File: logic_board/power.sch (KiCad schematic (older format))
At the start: 17 parts, among them J4 Amphenol 124015, J5 Batt, SW5 Power, U4 SPX3819M5-L-3-3, U5 BQ24090DGQR

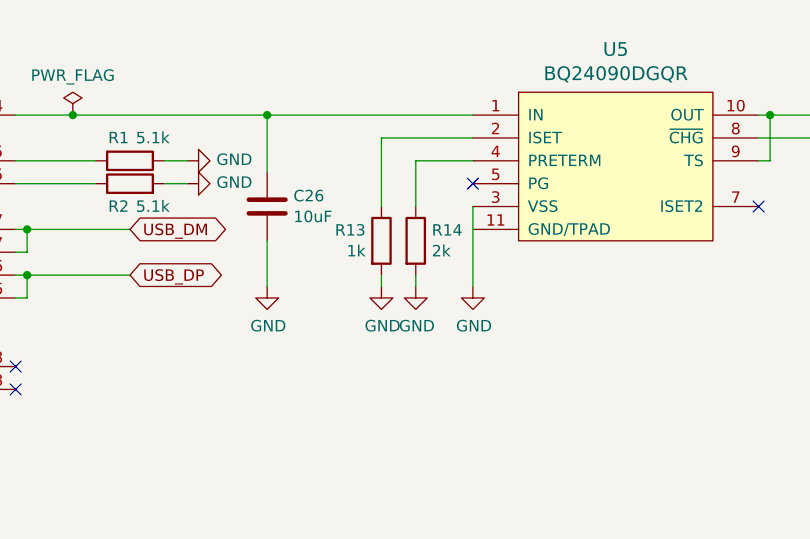
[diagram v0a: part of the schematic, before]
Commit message: Connect the thermal pad of the charger per datasheet recommendations
- Added a separate pin 11 for the thermal pad in the custom symbol.
- Ground the thermal pad.
- Add a bunch of vias to conduct heat through the board.
- Add a copper pour on the back side of the board to radiate heat.

Although the backside pour is at ground potential, I have added keepouts
around all ground via in its area to avoid ground loops.
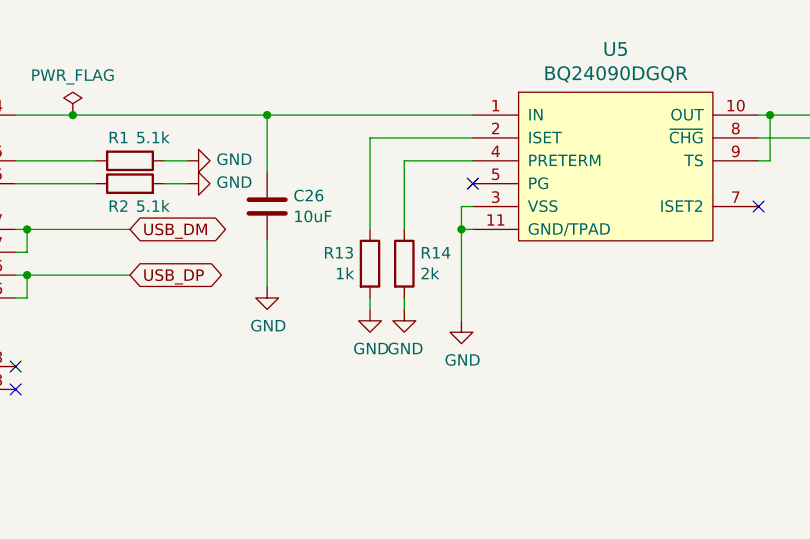
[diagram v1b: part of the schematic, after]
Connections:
- net GND: now also U5.11 (GND/TPAD)
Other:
- moved on the sheet: R13, R14
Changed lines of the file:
@@
 L Device:R R14
 U 1 1 5E283C3D
-P 5250 2550
-F 0 "R14" H 5320 2596 50  0000 L CNN
-F 1 "2k" H 5320 2505 50  0000 L CNN
-F 2 "Resistors_SMD:R_0402" V 5180 2550 50  0001 C CNN
-F 3 "~" H 5250 2550 50  0001 C CNN
-	1    5250 2550
+P 5200 2650
+F 0 "R14" H 5270 2696 50  0000 L CNN
+F 1 "2k" H 5270 2605 50  0000 L CNN
+F 2 "Resistors_SMD:R_0402" V 5130 2650 50  0001 C CNN
+F 3 "~" H 5200 2650 50  0001 C CNN
+	1    5200 2650
 	1    0    0    -1
 $EndComp
@@
 L Device:R R13
 U 1 1 5E288253
-P 5100 2550
-F 0 "R13" H 5031 2596 50  0000 R CNN
-F 1 "1k" H 5031 2505 50  0000 R CNN
-F 2 "Resistors_SMD:R_0402" V 5030 2550 50  0001 C CNN
-F 3 "~" H 5100 2550 50  0001 C CNN
-	1    5100 2550
+P 5050 2650
+F 0 "R13" H 4981 2696 50  0000 R CNN
+F 1 "1k" H 4981 2605 50  0000 R CNN
+F 2 "Resistors_SMD:R_0402" V 4980 2650 50  0001 C CNN
+F 3 "~" H 5050 2650 50  0001 C CNN
+	1    5050 2650
 	1    0    0    -1
 $EndComp
@@
 L power:GND #PWR033
 U 1 1 5E289703
-P 5100 2750
-F 0 "#PWR033" H 5100 2500 50  0001 C CNN
-F 1 "GND" H 5105 2577 50  0000 C CNN
-F 2 "" H 5100 2750 50  0001 C CNN
-F 3 "" H 5100 2750 50  0001 C CNN
-	1    5100 2750
+P 5050 2850
+F 0 "#PWR033" H 5050 2600 50  0001 C CNN
+F 1 "GND" H 5055 2677 50  0000 C CNN
+F 2 "" H 5050 2850 50  0001 C CNN
+F 3 "" H 5050 2850 50  0001 C CNN
+	1    5050 2850
 	1    0    0    -1
 $EndComp
@@
 L power:GND #PWR034
 U 1 1 5E289BF1
-P 5250 2750
-F 0 "#PWR034" H 5250 2500 50  0001 C CNN
-F 1 "GND" H 5255 2577 50  0000 C CNN
-F 2 "" H 5250 2750 50  0001 C CNN
-F 3 "" H 5250 2750 50  0001 C CNN
-	1    5250 2750
+P 5200 2850
+F 0 "#PWR034" H 5200 2600 50  0001 C CNN
+F 1 "GND" H 5205 2677 50  0000 C CNN
+F 2 "" H 5200 2850 50  0001 C CNN
+F 3 "" H 5200 2850 50  0001 C CNN
+	1    5200 2850
 	1    0    0    -1
 $EndComp
@@
 L power:GND #PWR035
 U 1 1 5E2AE842
-P 5500 2750
-F 0 "#PWR035" H 5500 2500 50  0001 C CNN
-F 1 "GND" H 5505 2577 50  0000 C CNN
-F 2 "" H 5500 2750 50  0001 C CNN
-F 3 "" H 5500 2750 50  0001 C CNN
-	1    5500 2750
-	1    0    0    -1
-$EndComp
-Wire Wire Line
-	5100 2100 5100 2400
-Wire Wire Line
-	5250 2200 5250 2400
+P 5450 2900
+F 0 "#PWR035" H 5450 2650 50  0001 C CNN
+F 1 "GND" H 5455 2727 50  0000 C CNN
+F 2 "" H 5450 2900 50  0001 C CNN
+F 3 "" H 5450 2900 50  0001 C CNN
+	1    5450 2900
+	1    0    0    -1
+$EndComp
 NoConn ~ 5500 2300
 Wire Wire Line
-	5100 2750 5100 2700
-Wire Wire Line
-	5250 2750 5250 2700
-Wire Wire Line
-	5500 2400 5500 2750
+	5050 2850 5050 2800
+Wire Wire Line
+	5200 2850 5200 2800
 $Comp
 L Device:LED D1
@@
 Wire Wire Line
 	4600 2000 5500 2000
-Wire Wire Line
-	5100 2100 5500 2100
-Wire Wire Line
-	5250 2200 5500 2200
 $Comp
 L power:PWR_FLAG #FLG01
@@
 Wire Wire Line
 	4200 4800 4400 4800
-$Comp
-L Device:CP C25
-U 1 1 5E395196
-P 4400 4950
-F 0 "C25" H 4518 4996 50  0000 L CNN
-F 1 "22uF" H 4518 4905 50  0000 L CNN
-F 2 "Capacitors_SMD:CP_Elec_6.3x4.5" H 4438 4800 50  0001 C CNN
-F 3 "~" H 4400 4950 50  0001 C CNN
-	1    4400 4950
-	1    0    0    -1
-$EndComp
 $Comp
 L power:GND #PWR037
@@
 Wire Wire Line
 	6700 5550 6700 5450
+$Comp
+L Device:CP C25
+U 1 1 5E395196
+P 4400 4950
+F 0 "C25" H 4518 4996 50  0000 L CNN
+F 1 "22uF" H 4518 4905 50  0000 L CNN
+F 2 "Capacitors_SMD:CP_Elec_6.3x4.5" H 4438 4800 50  0001 C CNN
+F 3 "~" H 4400 4950 50  0001 C CNN
+	1    4400 4950
+	1    0    0    -1
+$EndComp
+Wire Wire Line
+	5500 2400 5450 2400
+Wire Wire Line
+	5450 2400 5450 2500
+Wire Wire Line
+	5500 2500 5450 2500
+Connection ~ 5450 2500
+Wire Wire Line
+	5450 2500 5450 2900
+Wire Wire Line
+	5200 2200 5200 2500
+Wire Wire Line
+	5200 2200 5500 2200
+Wire Wire Line
+	5050 2100 5050 2500
+Wire Wire Line
+	5050 2100 5500 2100
 $EndSCHEMATC

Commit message: Update to symbols from newest KiCad
LEDs were also on the wrong side of the board.
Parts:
- C25, C3: footprint Capacitors_SMD:CP_Elec_6.3x4.5 -> Capacitor_SMD:CP_Elec_6.3x4.5
- C26: footprint Capacitors_SMD:C_0805_HandSoldering -> Capacitor_SMD:C_0805_2012Metric_Pad1.15x1.40mm_HandSolder
- C9: footprint Capacitors_SMD:C_0402 -> Capacitor_SMD:C_0402_1005Metric
- D1, D2: footprint LEDs:LED_D3.0mm_Horizontal_O1.27mm_Z2.0mm -> LED_THT:LED_D3.0mm_Horizontal_O1.27mm_Z2.0mm
- J4: footprint Connectors_USB:USB_C_Receptacle_Amphenol_12401610E4-2A -> Connector_USB:USB_C_Receptacle_Amphenol_12401610E4-2A
- R1, R13, R14, R16, R17, R2: footprint Resistors_SMD:R_0402 -> Resistor_SMD:R_0402_1005Metric
- U4: footprint TO_SOT_Packages_SMD:SOT-23-5_HandSoldering -> Package_TO_SOT_SMD:SOT-23-5_HandSoldering
- U5: footprint Housings_SSOP:MSOP-10-1EP_3x3mm_Pitch0.5mm -> Package_SO:MSOP-10-1EP_3x3mm_P0.5mm_EP1.68x1.88mm
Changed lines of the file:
@@
 F 0 "U5" H 6125 2787 60  0000 C CNN
 F 1 "BQ24090DGQR" H 6125 2681 60  0000 C CNN
-F 2 "Housings_SSOP:MSOP-10-1EP_3x3mm_Pitch0.5mm" H 5850 1900 60  0001 C CNN
+F 2 "Package_SO:MSOP-10-1EP_3x3mm_P0.5mm_EP1.68x1.88mm" H 5850 1900 60  0001 C CNN
 F 3 "http://www.ti.com/lit/ds/symlink/bq24092.pdf" H 6150 2250 60  0001 C CNN
 	1    6150 2250
@@
 F 0 "J4" H 3007 3467 50  0000 C CNN
 F 1 "Amphenol 124015" H 3007 3376 50  0000 C CNN
-F 2 "Connectors_USB:USB_C_Receptacle_Amphenol_12401610E4-2A" H 3050 2600 50  0001 C CNN
+F 2 "Connector_USB:USB_C_Receptacle_Amphenol_12401610E4-2A" H 3050 2600 50  0001 C CNN
 F 3 "https://www.usb.org/sites/default/files/documents/usb_type-c.zip" H 3050 2600 50  0001 C CNN
 	1    2900 2600
@@
 F 0 "R14" H 5270 2696 50  0000 L CNN
 F 1 "2k" H 5270 2605 50  0000 L CNN
-F 2 "Resistors_SMD:R_0402" V 5130 2650 50  0001 C CNN
+F 2 "Resistor_SMD:R_0402_1005Metric" V 5130 2650 50  0001 C CNN
 F 3 "~" H 5200 2650 50  0001 C CNN
 	1    5200 2650
@@
 F 0 "R13" H 4981 2696 50  0000 R CNN
 F 1 "1k" H 4981 2605 50  0000 R CNN
-F 2 "Resistors_SMD:R_0402" V 4980 2650 50  0001 C CNN
+F 2 "Resistor_SMD:R_0402_1005Metric" V 4980 2650 50  0001 C CNN
 F 3 "~" H 5050 2650 50  0001 C CNN
 	1    5050 2650
@@
 F 0 "D1" V 7289 2232 50  0000 R CNN
 F 1 "LED" V 7198 2232 50  0001 R CNN
-F 2 "LEDs:LED_D3.0mm_Horizontal_O1.27mm_Z2.0mm" H 7250 2350 50  0001 C CNN
+F 2 "LED_THT:LED_D3.0mm_Horizontal_O1.27mm_Z2.0mm" H 7250 2350 50  0001 C CNN
 F 3 "~" H 7250 2350 50  0001 C CNN
 F 4 "Charging" V 7200 2100 50  0000 C CNN "Name"
@@
 F 0 "R17" H 7320 2846 50  0000 L CNN
 F 1 "1.5k" H 7320 2755 50  0000 L CNN
-F 2 "Resistors_SMD:R_0402" V 7180 2800 50  0001 C CNN
+F 2 "Resistor_SMD:R_0402_1005Metric" V 7180 2800 50  0001 C CNN
 F 3 "~" H 7250 2800 50  0001 C CNN
 	1    7250 2800
@@
 F 0 "C26" H 4715 2446 50  0000 L CNN
 F 1 "10uF" H 4715 2355 50  0000 L CNN
-F 2 "Capacitors_SMD:C_0805_HandSoldering" H 4638 2250 50  0001 C CNN
+F 2 "Capacitor_SMD:C_0805_2012Metric_Pad1.15x1.40mm_HandSolder" H 4638 2250 50  0001 C CNN
 F 3 "~" H 4600 2400 50  0001 C CNN
 	1    4600 2400
@@
 F 0 "C3" H 6018 4996 50  0000 L CNN
 F 1 "22uF" H 6018 4905 50  0000 L CNN
-F 2 "Capacitors_SMD:CP_Elec_6.3x4.5" H 5938 4800 50  0001 C CNN
+F 2 "Capacitor_SMD:CP_Elec_6.3x4.5" H 5938 4800 50  0001 C CNN
 F 3 "~" H 5900 4950 50  0001 C CNN
 	1    5900 4950
@@
 F 0 "D2" V 6384 4832 50  0000 R CNN
 F 1 "LED" V 6293 4832 50  0000 R CNN
-F 2 "LEDs:LED_D3.0mm_Horizontal_O1.27mm_Z2.0mm" H 6300 4950 50  0001 C CNN
+F 2 "LED_THT:LED_D3.0mm_Horizontal_O1.27mm_Z2.0mm" H 6300 4950 50  0001 C CNN
 F 3 "~" H 6300 4950 50  0001 C CNN
 F 4 "Power" V 6202 4832 50  0000 R CNN "Name"
@@
 F 0 "R16" H 6230 5396 50  0000 R CNN
 F 1 "1.5k" H 6230 5305 50  0000 R CNN
-F 2 "Resistors_SMD:R_0402" V 6230 5350 50  0001 C CNN
+F 2 "Resistor_SMD:R_0402_1005Metric" V 6230 5350 50  0001 C CNN
 F 3 "~" H 6300 5350 50  0001 C CNN
 	1    6300 5350
@@
 F 0 "C9" H 7915 2346 50  0000 L CNN
 F 1 "10uF" H 7915 2255 50  0000 L CNN
-F 2 "Capacitors_SMD:C_0402" H 7838 2150 50  0001 C CNN
+F 2 "Capacitor_SMD:C_0402_1005Metric" H 7838 2150 50  0001 C CNN
 F 3 "~" H 7800 2300 50  0001 C CNN
 	1    7800 2300
@@
 F 0 "R1" V 3900 2150 50  0000 C CNN
 F 1 "5.1k" V 3900 2300 50  0000 C CNN
-F 2 "Resistors_SMD:R_0402" V 3930 2200 50  0001 C CNN
+F 2 "Resistor_SMD:R_0402_1005Metric" V 3930 2200 50  0001 C CNN
 F 3 "~" H 4000 2200 50  0001 C CNN
 	1    4000 2200
@@
 F 0 "R2" V 3900 2350 50  0000 C CNN
 F 1 "5.1k" V 3900 2200 50  0000 C CNN
-F 2 "Resistors_SMD:R_0402" V 3930 2300 50  0001 C CNN
+F 2 "Resistor_SMD:R_0402_1005Metric" V 3930 2300 50  0001 C CNN
 F 3 "~" H 4000 2300 50  0001 C CNN
 	1    4000 2300
@@
 F 0 "U4" H 5250 5242 50  0000 C CNN
 F 1 "SPX3819M5-L-3-3" H 5250 5151 50  0000 C CNN
-F 2 "TO_SOT_Packages_SMD:SOT-23-5_HandSoldering" H 5250 5225 50  0001 C CNN
+F 2 "Package_TO_SOT_SMD:SOT-23-5_HandSoldering" H 5250 5225 50  0001 C CNN
 F 3 "https://www.exar.com/content/document.ashx?id=22106&languageid=1033&type=Datasheet&partnumber=SPX3819&filename=SPX3819.pdf&part=SPX3819" H 5250 4900 50  0001 C CNN
 	1    5250 4900
@@
 F 0 "C25" H 4518 4996 50  0000 L CNN
 F 1 "22uF" H 4518 4905 50  0000 L CNN
-F 2 "Capacitors_SMD:CP_Elec_6.3x4.5" H 4438 4800 50  0001 C CNN
+F 2 "Capacitor_SMD:CP_Elec_6.3x4.5" H 4438 4800 50  0001 C CNN
 F 3 "~" H 4400 4950 50  0001 C CNN
 	1    4400 4950

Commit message: Use through-hole USB C connector for easier soldering.
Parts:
- J4: footprint Connector_USB:USB_C_Receptacle_Amphenol_12401610E4-2A -> Connector_USB:USB_C_Receptacle_GCT_USB4085
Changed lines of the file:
@@
 F 0 "J4" H 3007 3467 50  0000 C CNN
 F 1 "Amphenol 124015" H 3007 3376 50  0000 C CNN
-F 2 "Connector_USB:USB_C_Receptacle_Amphenol_12401610E4-2A" H 3050 2600 50  0001 C CNN
+F 2 "Connector_USB:USB_C_Receptacle_GCT_USB4085" H 3050 2600 50  0001 C CNN
 F 3 "https://www.usb.org/sites/default/files/documents/usb_type-c.zip" H 3050 2600 50  0001 C CNN
 	1    2900 2600

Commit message: Update all 0402 SMD packages to 0603
Mainly to make soldering easier. 0402 was unnecessarily small.
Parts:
- C9: footprint Capacitor_SMD:C_0402_1005Metric -> Capacitor_SMD:C_0603_1608Metric_Pad1.05x0.95mm_HandSolder
- R1, R13, R14, R16, R17, R2: footprint Resistor_SMD:R_0402_1005Metric -> Resistor_SMD:R_0603_1608Metric_Pad1.05x0.95mm_HandSolder
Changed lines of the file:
@@
 F 0 "R14" H 5270 2696 50  0000 L CNN
 F 1 "2k" H 5270 2605 50  0000 L CNN
-F 2 "Resistor_SMD:R_0402_1005Metric" V 5130 2650 50  0001 C CNN
+F 2 "Resistor_SMD:R_0603_1608Metric_Pad1.05x0.95mm_HandSolder" V 5130 2650 50  0001 C CNN
 F 3 "~" H 5200 2650 50  0001 C CNN
 	1    5200 2650
@@
 F 0 "R13" H 4981 2696 50  0000 R CNN
 F 1 "1k" H 4981 2605 50  0000 R CNN
-F 2 "Resistor_SMD:R_0402_1005Metric" V 4980 2650 50  0001 C CNN
+F 2 "Resistor_SMD:R_0603_1608Metric_Pad1.05x0.95mm_HandSolder" V 4980 2650 50  0001 C CNN
 F 3 "~" H 5050 2650 50  0001 C CNN
 	1    5050 2650
@@
 F 0 "R17" H 7320 2846 50  0000 L CNN
 F 1 "1.5k" H 7320 2755 50  0000 L CNN
-F 2 "Resistor_SMD:R_0402_1005Metric" V 7180 2800 50  0001 C CNN
+F 2 "Resistor_SMD:R_0603_1608Metric_Pad1.05x0.95mm_HandSolder" V 7180 2800 50  0001 C CNN
 F 3 "~" H 7250 2800 50  0001 C CNN
 	1    7250 2800
@@
 F 0 "R16" H 6230 5396 50  0000 R CNN
 F 1 "1.5k" H 6230 5305 50  0000 R CNN
-F 2 "Resistor_SMD:R_0402_1005Metric" V 6230 5350 50  0001 C CNN
+F 2 "Resistor_SMD:R_0603_1608Metric_Pad1.05x0.95mm_HandSolder" V 6230 5350 50  0001 C CNN
 F 3 "~" H 6300 5350 50  0001 C CNN
 	1    6300 5350
@@
 F 0 "C9" H 7915 2346 50  0000 L CNN
 F 1 "10uF" H 7915 2255 50  0000 L CNN
-F 2 "Capacitor_SMD:C_0402_1005Metric" H 7838 2150 50  0001 C CNN
+F 2 "Capacitor_SMD:C_0603_1608Metric_Pad1.05x0.95mm_HandSolder" H 7838 2150 50  0001 C CNN
 F 3 "~" H 7800 2300 50  0001 C CNN
 	1    7800 2300
@@
 F 0 "R1" V 3900 2150 50  0000 C CNN
 F 1 "5.1k" V 3900 2300 50  0000 C CNN
-F 2 "Resistor_SMD:R_0402_1005Metric" V 3930 2200 50  0001 C CNN
+F 2 "Resistor_SMD:R_0603_1608Metric_Pad1.05x0.95mm_HandSolder" V 3930 2200 50  0001 C CNN
 F 3 "~" H 4000 2200 50  0001 C CNN
 	1    4000 2200
@@
 F 0 "R2" V 3900 2350 50  0000 C CNN
 F 1 "5.1k" V 3900 2200 50  0000 C CNN
-F 2 "Resistor_SMD:R_0402_1005Metric" V 3930 2300 50  0001 C CNN
+F 2 "Resistor_SMD:R_0603_1608Metric_Pad1.05x0.95mm_HandSolder" V 3930 2300 50  0001 C CNN
 F 3 "~" H 4000 2300 50  0001 C CNN
 	1    4000 2300
